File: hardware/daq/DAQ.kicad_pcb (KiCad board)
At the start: 4 copper layers, 112 x 125 mm, 190 parts, among them J1 ICD15S13E4GX00LF, J2 ICD15S13E4GX00LF, J4 ICD15S13E4GX00LF, J5 ICD15S13E4GX00LF, P1 0022272021, U1 ADS124S08IRHBT, U11 SN74AHCT125RGYR, U2 ADS124S08IRHBT, U3 LT6654BMPS6-5-TRMPBF, U4 LM1086IS-5.0_NOPB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

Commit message: ROUTED ADC3 BAYBEEE
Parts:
- removed the R27 at (112.1, 112.7)
- removed the R28 at (112.9, 142.8)
- added R43: 20K, CRCW060320K0FKEA:RESC1508X50N, F.Cu at (106.4, 111.7)
- moved C75 140.8 mm to (100.1, 109.9), turned to 180 degrees
- moved C76 138.7 mm to (100.9, 113.1), turned to 180 degrees
- moved C97 137.3 mm to (100.3, 105.9)
- moved R61 136.0 mm to (92.1, 107.3)
- moved C96 135.4 mm to (100.5, 97.5), turned to -90 degrees
- moved R51 133.4 mm to (110.6, 107.5)
- moved C77 133.4 mm to (113.1, 106.9)
- moved C78 133.4 mm to (115.1, 102.9)
- moved C80 133.4 mm to (115.1, 99.9)
- moved C83 133.4 mm to (115.1, 96.9)
- moved C87 133.4 mm to (105.1, 96.9)
- moved C88 133.4 mm to (109.1, 96.9)
- moved C89 133.4 mm to (105.1, 98.9)
- moved C90 133.4 mm to (109.1, 98.9)
- moved C91 133.4 mm to (105.1, 100.9)
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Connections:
- C86 pad 1: Net-(U9-AIN4) -> unconnected-(C86-Pad1)
- C86 pad 2: Net-(U9-AIN2) -> unconnected-(C86-Pad2)
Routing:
- net Net-(U9-AIN1): track 7.57 -> 31.3 mm
- net Net-(U9-REFP1_AIN6): track 2.43 -> 21.3 mm
- net Net-(U9-AIN0): track 10.2 -> 28.7 mm
- net GND: track 68.4 -> 85.1 mm, vias 16 -> 13
- net /IDAC1_3: track 2.38 -> 14.2 mm
- net /IDAC2_3: track 2.66 -> 13.8 mm, vias 1 -> 2
- net Net-(U9-AIN4): track 5.77 -> 15.7 mm
- net Net-(U9-REFN1_AIN7): track 7.87 -> 17.7 mm
- net Net-(U9-AIN2): track 3.18 -> 12.3 mm
- net /RESET_N2: track 8.85 -> 0.00 mm
- net Net-(U2-RESET_N): track 0.00 -> 7.67 mm, vias 1 -> 0
- net /RESET_N1: track 7.60 -> 0.00 mm
- net Net-(U1-RESET_N): track 0.00 -> 7.60 mm
- net /RTD3_L1: track 0.00 -> 6.00 mm
- net Net-(U9-GPIO2_AIN10): track 5.79 -> 11.1 mm
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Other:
- board text added: "DAQ + F3C Capstone 2025-2026 Jimmy Fowler"
- board text added: "U1"
- board text removed: "DAQ + F3C Capstone 2025-2026"

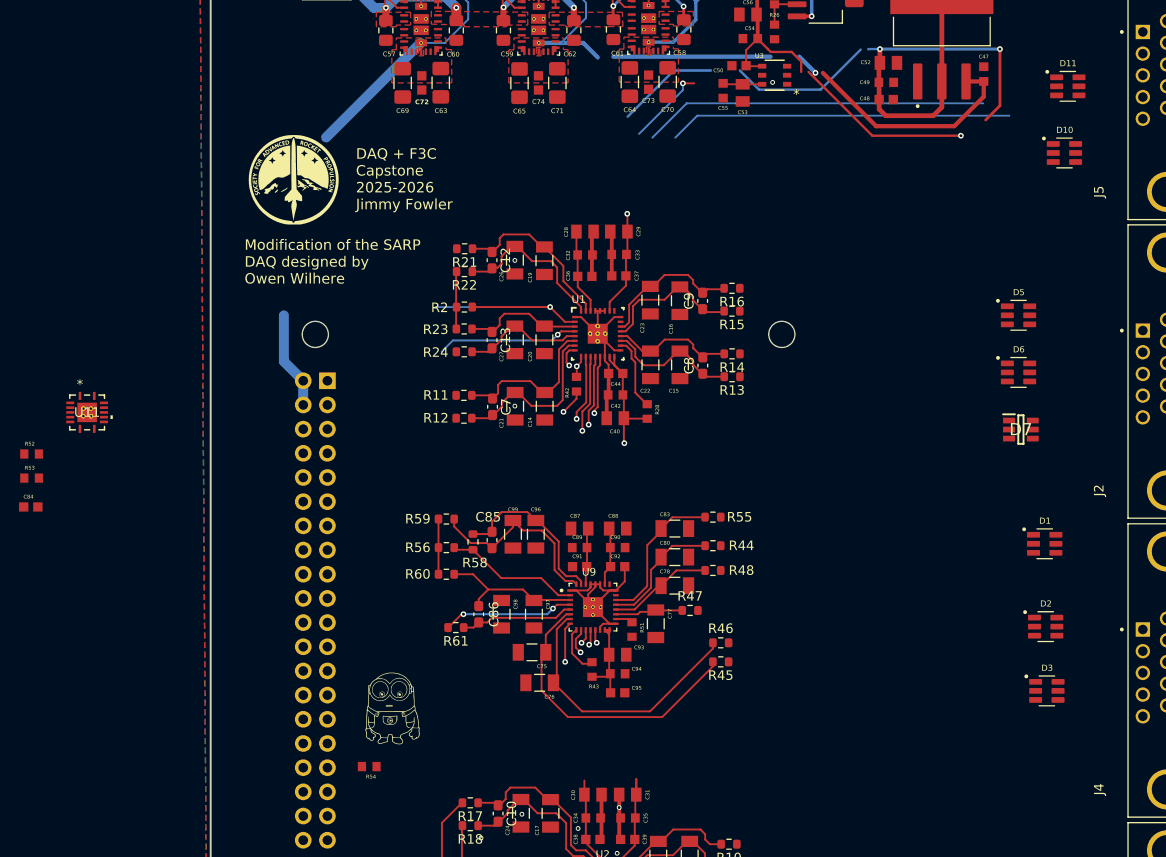
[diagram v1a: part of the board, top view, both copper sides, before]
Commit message: routed UART conversion components
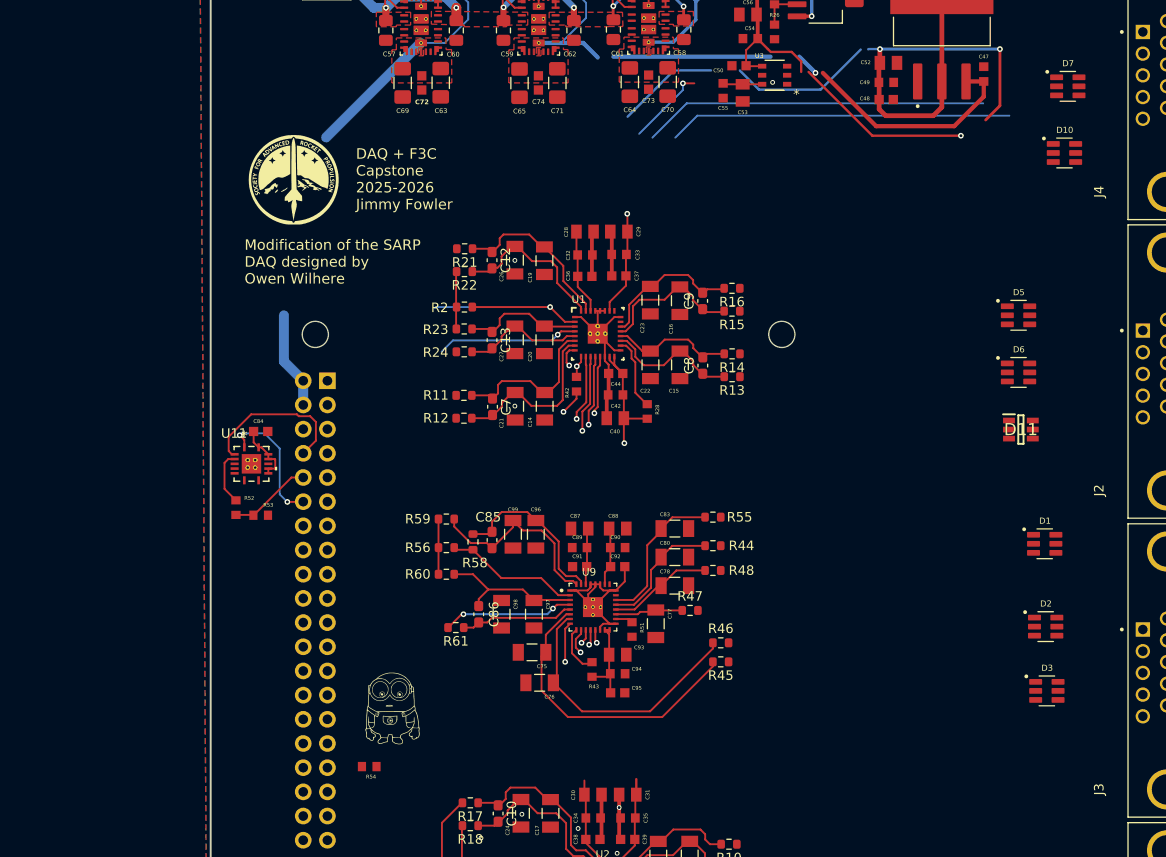
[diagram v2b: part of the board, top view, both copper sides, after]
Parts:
- R52: value 1K -> 10K
- R53: value 2.2K -> 20K
- moved C84 25.4 mm to (71.6, 86.7)
- moved R53 24.4 mm to (71.6, 95.5)
- moved R52 22.2 mm to (69.0, 94.7), turned to 90 degrees
- moved U11 18.1 mm to (70.6, 90.1)
- renumbered D7 to D11, D11 to D7, J4 to J3, J5 to J4
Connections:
- C86 pad 1: unconnected-(C86-Pad1) -> Net-(U9-AIN4)
- C86 pad 2: unconnected-(C86-Pad2) -> Net-(U9-AIN2)
- R54 pad 1: +3.3V -> /TX_ENABLE
- R54 pad 2: /TX_ENABLE -> +3.3V
- RP1 pad 11: /START_SYNC1 -> /DRDY_N3
- RP1 pad 12: /DRDY_N3 -> /TX_ENABLE
- RP1 pad 33: /TX_ENABLE -> /START_SYNC1
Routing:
- net /TX_PI: track 0.00 -> 16.6 mm
- net /TX_ENABLE: track 0.00 -> 14.0 mm, vias 0 -> 2
- net /RX_PI: track 0.00 -> 8.75 mm
- net +5Vs: track 102.3 -> 108.9 mm
- net /DATA_BUS: track 0.00 -> 5.66 mm

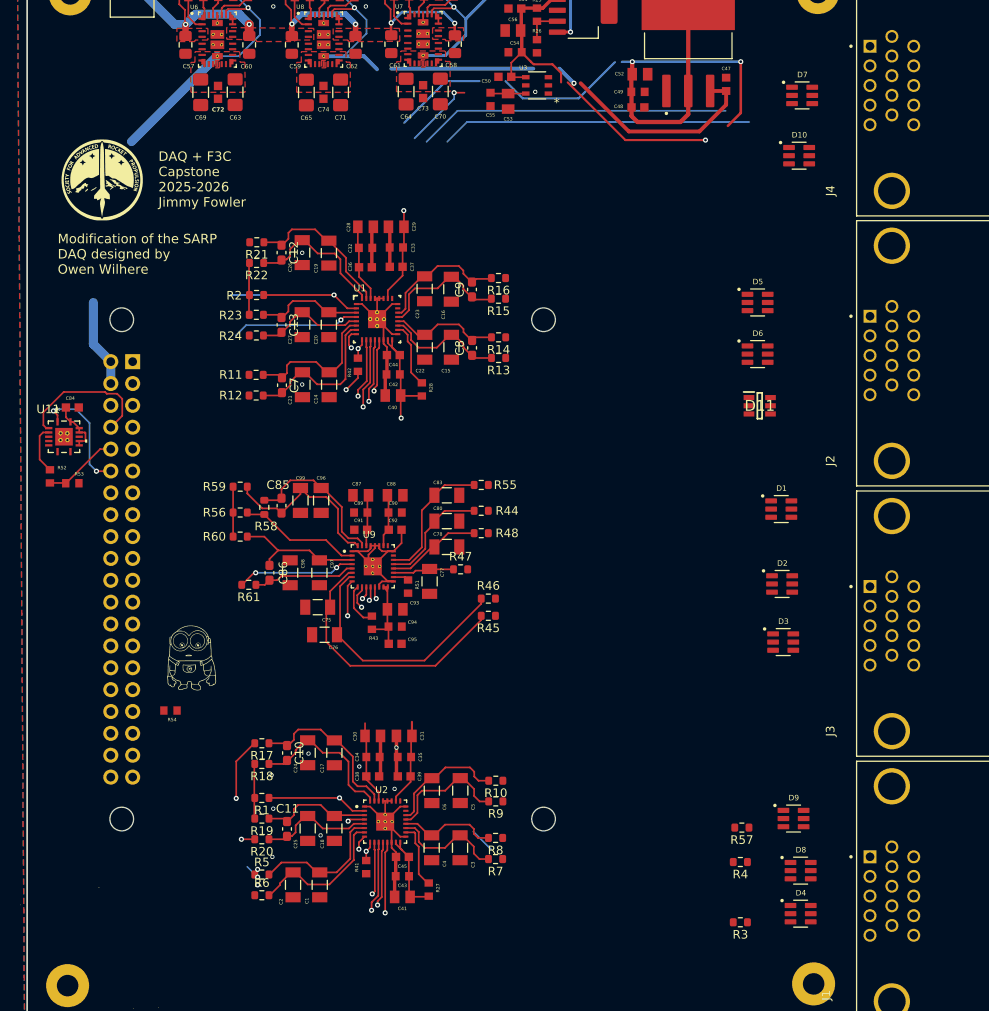
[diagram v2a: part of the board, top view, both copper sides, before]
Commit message: routed 1.75 DSUBs
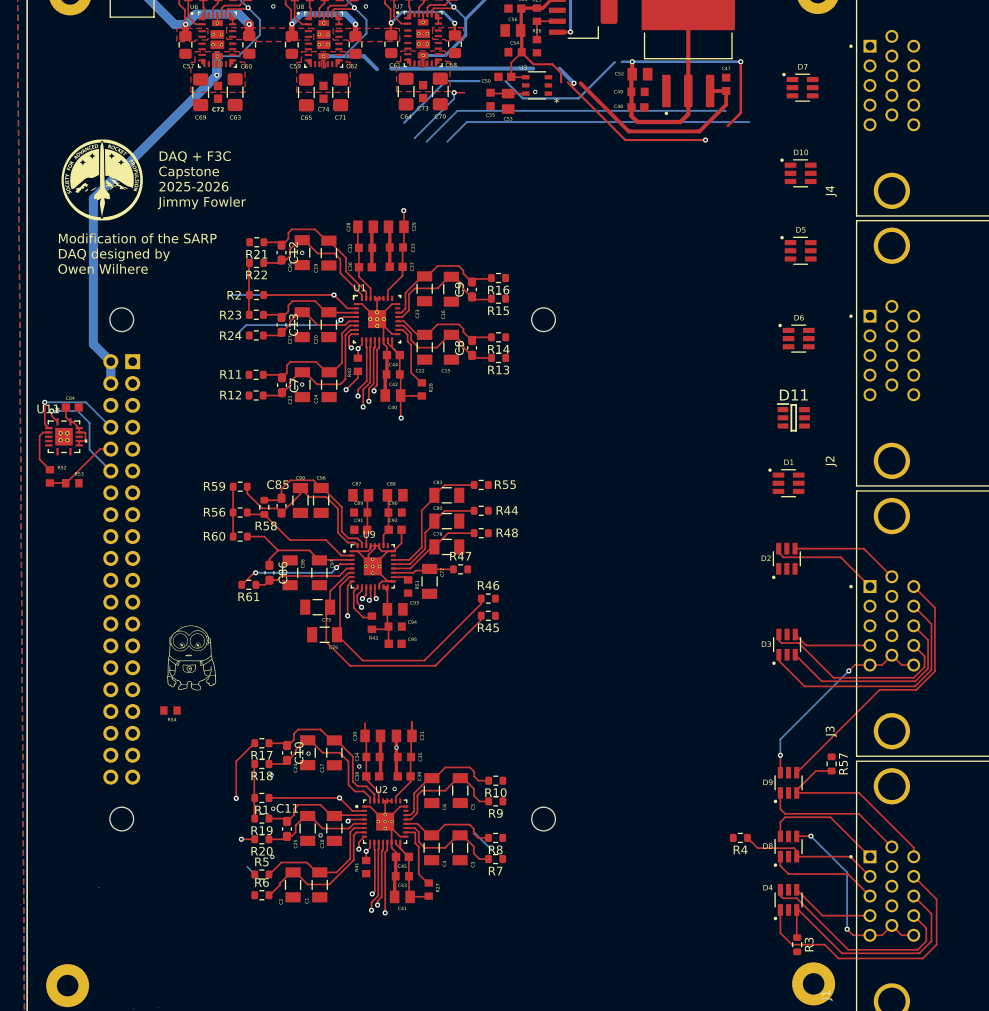
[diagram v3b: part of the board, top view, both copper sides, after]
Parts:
- moved R57 12.8 mm to (159.8, 128.1), turned to 90 degrees
- moved D5 7.81 mm to (156.2, 68.5)
- moved R3 7.09 mm to (155.8, 149.1), turned to -90 degrees
- moved D6 5.10 mm to (155.9, 78.7)
- moved D11 4.19 mm to (155.4, 87.9)
- moved D9 4.19 mm to (154.8, 130.3), turned to 90 degrees
- moved D8 3.13 mm to (154.8, 137.7), turned to 90 degrees
- moved D1 3.12 mm to (154.8, 95.5)
- moved D2 2.98 mm to (154.6, 104.3), turned to 90 degrees
- moved R4 2.80 mm to (149.2, 136.7)
- moved D4 2.13 mm to (154.8, 143.9), turned to 90 degrees
- moved D10 2.06 mm to (156.2, 59.5)
- moved D7 0.90 mm to (156.4, 49.5)
- moved D3 0.54 mm to (154.6, 114.2), turned to 90 degrees
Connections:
- D1 pad 6: /PT7_SIG -> /PT9_SIG
- D10 pad 4: unconnected-(D10-Pad4) -> /FMV
- D2 pad 1: /PT3_SIG -> unconnected-(D2-Pad1)
- D2 pad 6: /PT9_SIG -> /PT7_SIG
- D3 pad 4: /PT12_SIG -> /PT11_SIG
- D3 pad 6: /PT11_SIG -> /PT12_SIG
- D9 pad 4: /FMV -> /PT3_SIG
- J1 pad 1: /RTD1_L3 -> /RTD1_L1
- J1 pad 11: /IDAC2_2 -> /RTD3_L3
- J1 pad 12: /RTD2_L3 -> /IDAC2_2
- J1 pad 13: /RTD2_L1 -> /RTD2_L3
- J1 pad 14: /RTD3_L3 -> /RTD2_L1
- J1 pad 2: /RTD1_L1 -> /RTD1_L3
- J3 pad 11: /PT12_SIG -> /PT3_SIG
- J3 pad 14: /PT3_SIG -> /PT12_SIG
- J3 pad 4: /PT10_SIG -> /PT11_SIG
- J3 pad 6: /PT11_SIG -> /PT10_SIG
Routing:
- net +5Vs: track 108.9 -> 155.9 mm, vias 3 -> 7
- net /PT3_SIG: track 0.00 -> 31.8 mm
- net /IDAC2_2: track 3.48 -> 35.2 mm
- net /PT1_SIG: track 1.70 -> 30.4 mm, vias 2 -> 0
- net /RTD2_L3: track 0.00 -> 27.6 mm
- net /RTD2_L1: track 6.35 -> 30.6 mm
- net /PT2_SIG: track 0.10 -> 23.1 mm
- net /PT12_SIG: track 0.00 -> 23.0 mm
- net /RTD3_L3: track 0.00 -> 22.6 mm
- net +5V: track 44.6 -> 65.7 mm, vias 2 -> 3
- net /IDAC2_3: track 13.8 -> 30.5 mm
- net /RTD1_L3: track 0.00 -> 16.5 mm
- net /RTD1_L1: track 42.3 -> 56.5 mm
- net /IDAC2_1: track 50.9 -> 63.9 mm
- net /PT7_SIG: track 0.00 -> 12.7 mm
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- added copper zone on In1.Cu, net GND
- added copper zone on In2.Cu, net GND

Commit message: 2 DSUBs???
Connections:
- J1 pad 1: /RTD1_L1 -> /PT4_SIG
- J1 pad 2: /RTD1_L3 -> /PT5_SIG
- J1 pad 3: /IDAC2_1 -> /PT6_SIG
- J2 pad 12: /PT4_SIG -> /RTD1_L1
- J2 pad 13: /PT5_SIG -> /RTD1_L3
- J2 pad 14: /PT6_SIG -> /IDAC2_1
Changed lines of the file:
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@@
 			(layers "*.Cu" "*.Mask")
 			(remove_unused_layers no)
-			(net 44 "/PT4_SIG")
+			(net 37 "/RTD1_L1")
 			(pinfunction "12")
 			(pintype "passive")
@@
 			(layers "*.Cu" "*.Mask")
 			(remove_unused_layers no)
-			(net 46 "/PT5_SIG")
+			(net 120 "/RTD1_L3")
 			(pinfunction "13")
 			(pintype "passive")
@@
 			(layers "*.Cu" "*.Mask")
 			(remove_unused_layers no)
-			(net 47 "/PT6_SIG")
+			(net 39 "/IDAC2_1")
 			(pinfunction "14")
 			(pintype "passive")
@@
 		(at 166.774699 143.182691 90)
 		(property "Reference" "J1"
-			(at -11.765559 -7.627199 90)
+			(at -11.705 -5.4 90)
 			(layer "F.SilkS")
 			(effects
@@
 			(layers "*.Cu" "*.Mask")
 			(remove_unused_layers no)
-			(net 37 "/RTD1_L1")
+			(net 44 "/PT4_SIG")
 			(pinfunction "1")
 			(pintype "passive")
@@
 			(layers "*.Cu" "*.Mask")
 			(remove_unused_layers no)
-			(net 120 "/RTD1_L3")
+			(net 46 "/PT5_SIG")
 			(pinfunction "2")
 			(pintype "passive")
@@
 			(layers "*.Cu" "*.Mask")
 			(remove_unused_layers no)
-			(net 39 "/IDAC2_1")
+			(net 47 "/PT6_SIG")
 			(pinfunction "3")
 			(pintype "passive")
